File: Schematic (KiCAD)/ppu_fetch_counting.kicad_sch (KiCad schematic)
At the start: 28 parts

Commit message: - Started work on the pulse channels.  - Solved at least 2 of the red traces in the SVG.  - Finally realized that "Unknown 4to1" cells are actually just ordinary And-Or-Invert "AOI22" cells.
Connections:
- net at S7. (X): now also R9. (X); no longer S8. (/Q)
- net at S19. (X): now also R12. (X); no longer S20. (/Q)
- net at S11. (X): now also R10. (X); no longer S12. (/Q)
- net at S14. (X): now also R11. (X); no longer S15. (/Q)
- new net: S10. (X), S12. (/Q), S8. (/Q)
- new net: S22. (X), S23. (/Q), S26. (/Q), S27. (/Q), S28. (/Q)
- new net: S7. (X), S8. (/Q)
- new net: S19. (X), S20. (/Q)
- new net: S12. (/Q), S13. (X), S15. (/Q)
- new net: S11. (X), S12. (/Q)
- new net: R5. (/Q), S16. (X)
- new net: S14. (X), S15. (/Q)
- new net: S20. (/Q), S21. (X), S23. (/Q)

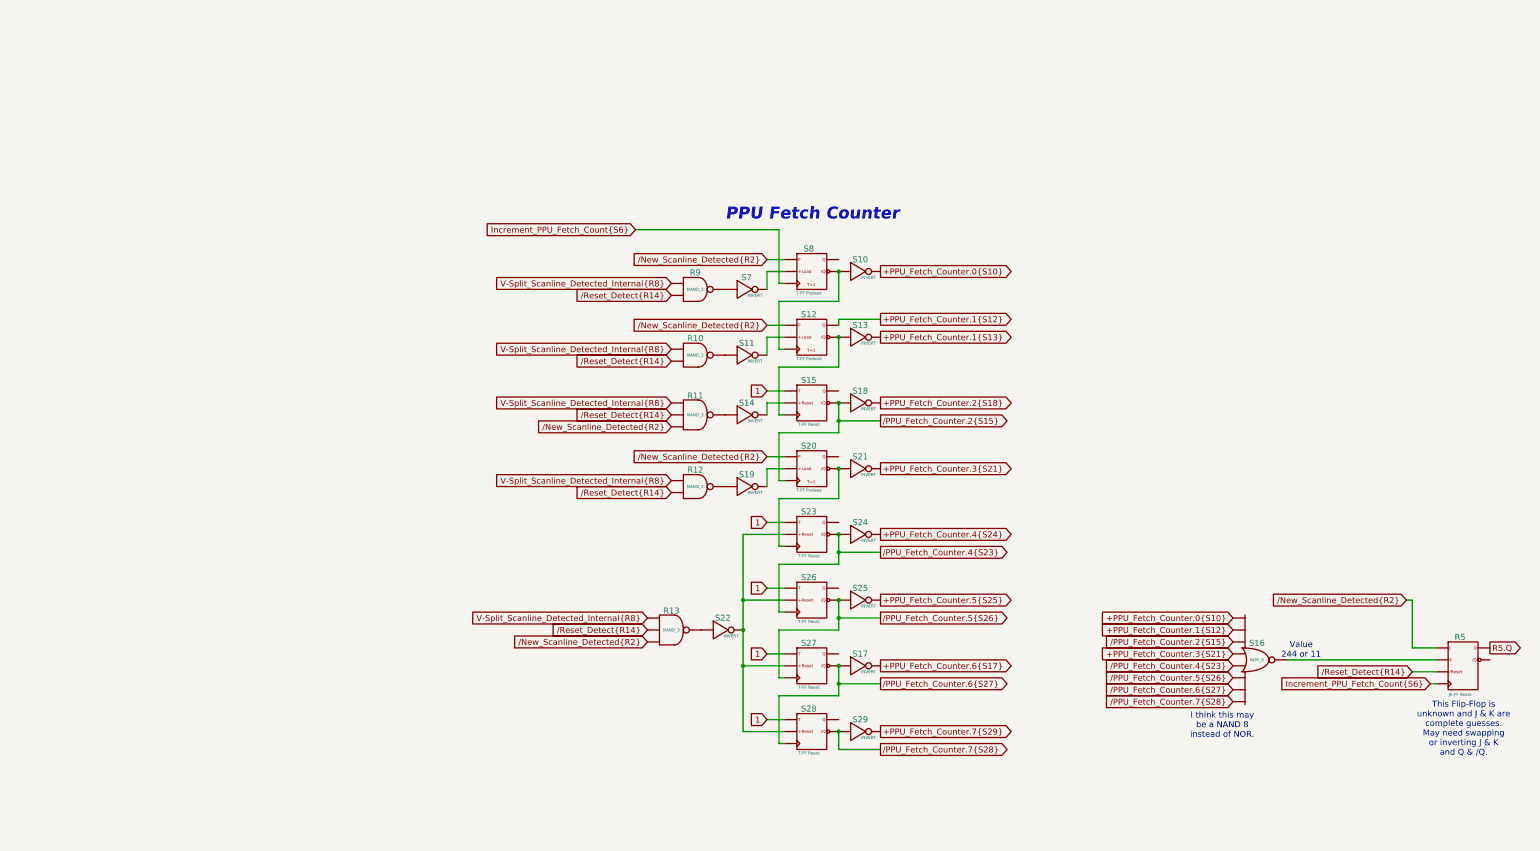
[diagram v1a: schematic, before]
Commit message: - All cells in the left and center areas have now been added into the schematics.  - Changed naming of the PDF files; I was accidentally writing over furrtek's original with my new PDF.
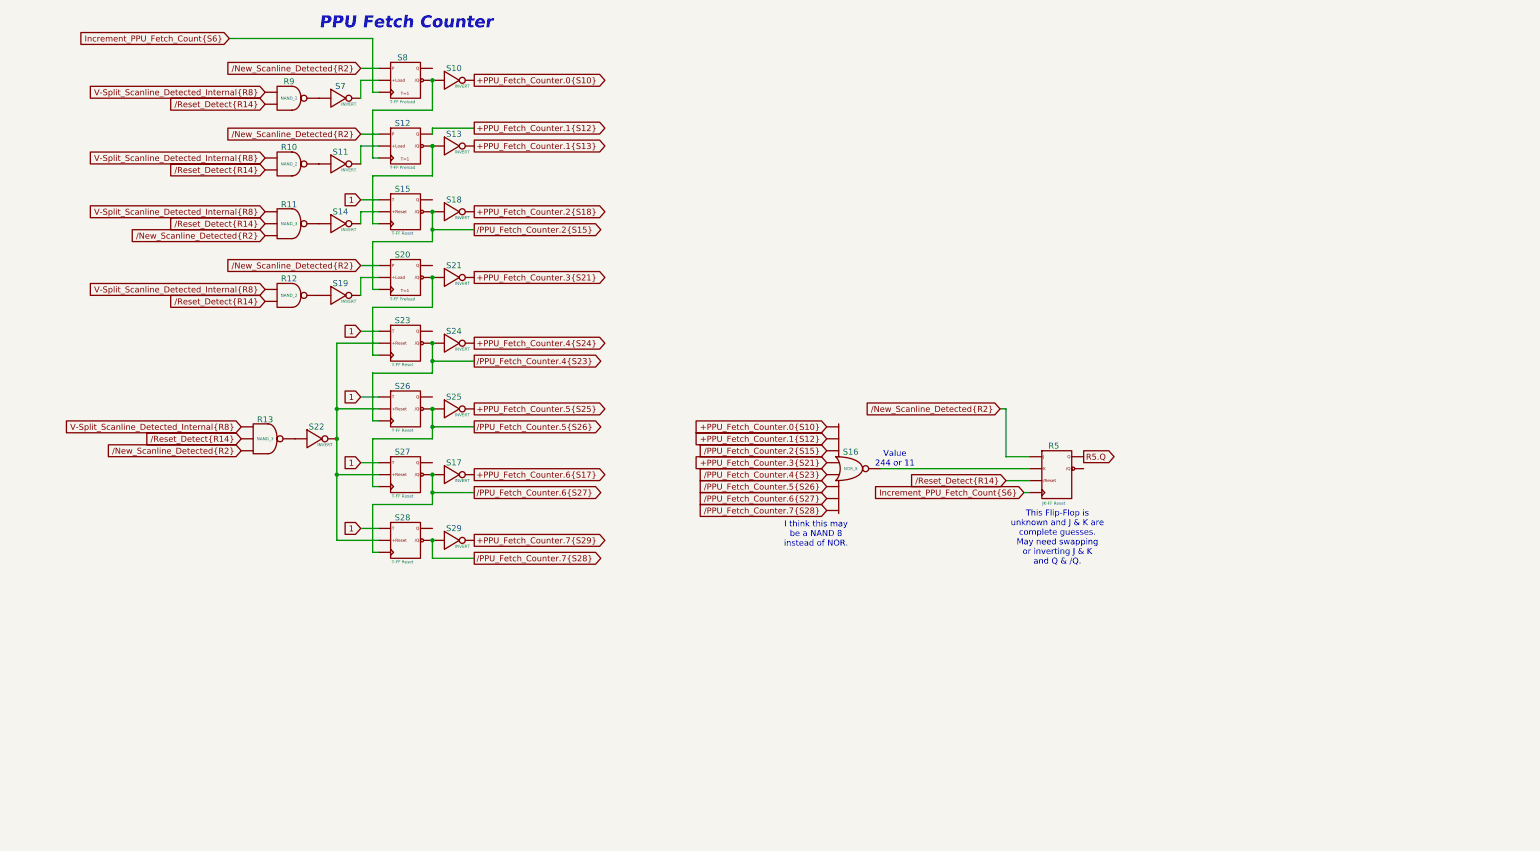
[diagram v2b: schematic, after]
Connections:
- net at S7. (X): now also R9. (X); no longer S8. (/Q)
- net at S19. (X): now also R12. (X); no longer S20. (/Q)
- net at S11. (X): now also R10. (X); no longer S12. (/Q)
- net at S14. (X): now also R11. (X); no longer S15. (/Q)
- new net: S10. (X), S12. (/Q), S8. (/Q)
- new net: S22. (X), S23. (/Q), S26. (/Q), S27. (/Q), S28. (/Q)
- new net: S7. (X), S8. (/Q)
- new net: S19. (X), S20. (/Q)
- new net: S12. (/Q), S13. (X), S15. (/Q)
- new net: S11. (X), S12. (/Q)
- new net: R5. (/Q), S16. (X)
- new net: S14. (X), S15. (/Q)
- new net: S20. (/Q), S21. (X), S23. (/Q)
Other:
- moved on the sheet: R10, R11, R12, R13, R5, R9, S10, S11, S12, S13, S14, S15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

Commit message: - All known gates and traces are now accounted for in the schematics!  :)
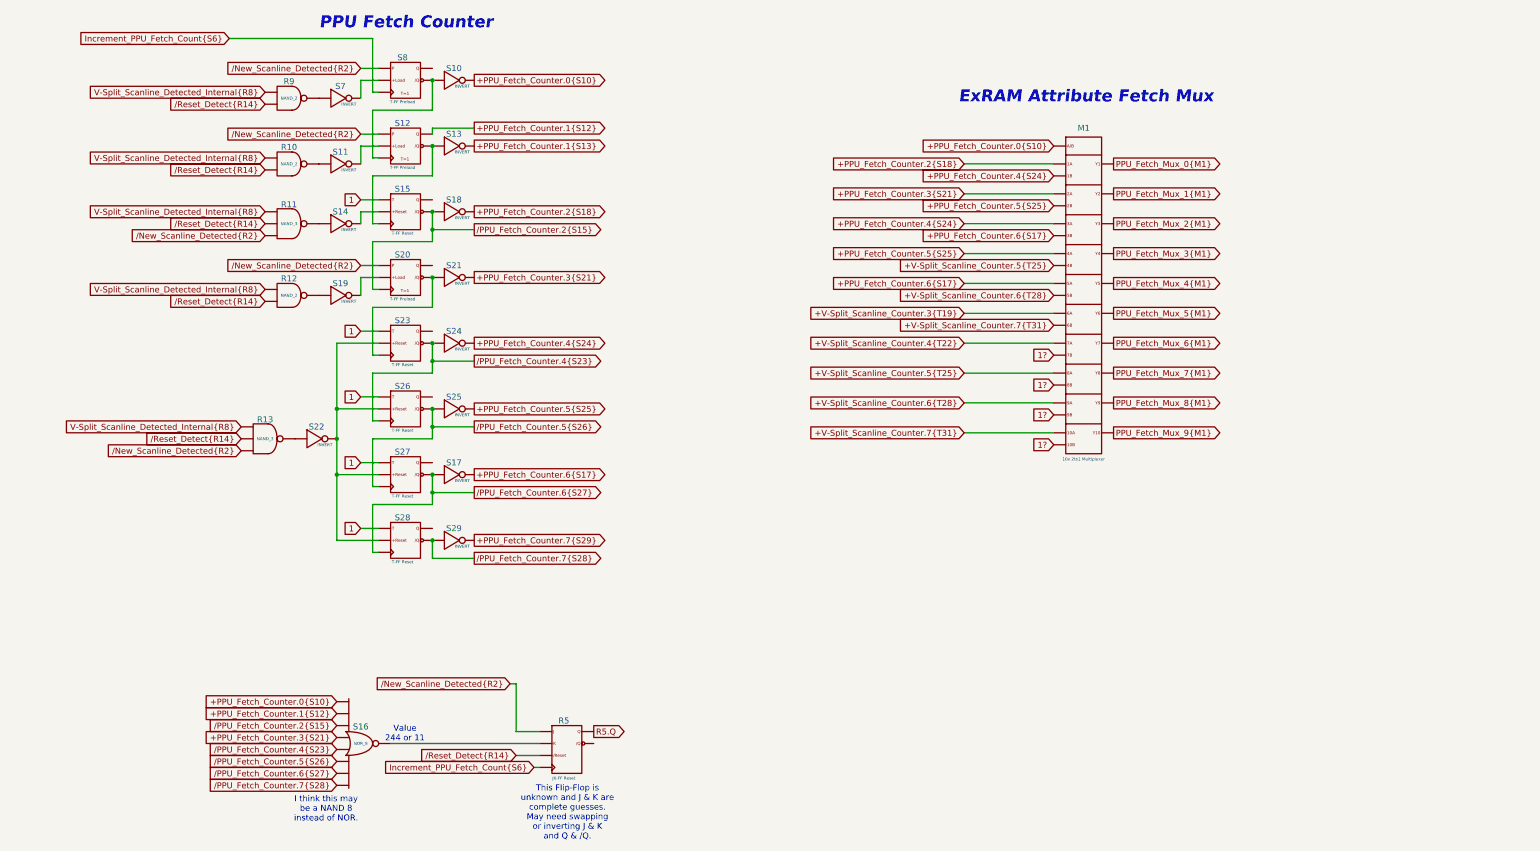
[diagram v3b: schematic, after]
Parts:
- added M1: 10x 2to1 Multiplexer, symbol MMC5:Multiplexer_10x2to1
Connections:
- net +PPU_Fetch_Counter.0{S10}: now also M1. (Y10)
- net +PPU_Fetch_Counter.2{S18}: now also M1. (Y10)
- net +PPU_Fetch_Counter.3{S21}: now also M1. (Y10)
- net +PPU_Fetch_Counter.4{S24}: now also M1. (Y10)
- net +PPU_Fetch_Counter.5{S25}: now also M1. (Y10)
- net +PPU_Fetch_Counter.6{S17}: now also M1. (Y10)
- net at S7. (X): now also R9. (X); no longer S8. (/Q)
- net at S19. (X): now also R12. (X); no longer S20. (/Q)
- net at S11. (X): now also R10. (X); no longer S12. (/Q)
- net at S14. (X): now also R11. (X); no longer S15. (/Q)
- new net: S10. (X), S12. (/Q), S8. (/Q)
- new net: S22. (X), S23. (/Q), S26. (/Q), S27. (/Q), S28. (/Q)
- new net: S7. (X), S8. (/Q)
- new net: S19. (X), S20. (/Q)
- new net: S12. (/Q), S13. (X), S15. (/Q)
- new net: S11. (X), S12. (/Q)
- new net: R5. (/Q), S16. (X)
- new net: S14. (X), S15. (/Q)
- new net: S20. (/Q), S21. (X), S23. (/Q)
- new net +V-Split_Scanline_Counter.3{T19}: M1. (Y10)
- new net +V-Split_Scanline_Counter.4{T22}: M1. (Y10)
- new net +V-Split_Scanline_Counter.5{T25}: M1. (Y10)
- new net +V-Split_Scanline_Counter.6{T28}: M1. (Y10)
- new net +V-Split_Scanline_Counter.7{T31}: M1. (Y10)
- new net 1?: M1. (Y10)
- new net PPU_Fetch_Mux_0{M1}: M1. (Y10)
- new net PPU_Fetch_Mux_1{M1}: M1. (Y10)
- new net PPU_Fetch_Mux_2{M1}: M1. (Y10)
- new net PPU_Fetch_Mux_3{M1}: M1. (Y10)
- new net PPU_Fetch_Mux_4{M1}: M1. (Y10)
- new net PPU_Fetch_Mux_5{M1}: M1. (Y10)
- new net PPU_Fetch_Mux_6{M1}: M1. (Y10)
- new net PPU_Fetch_Mux_7{M1}: M1. (Y10)
- new net PPU_Fetch_Mux_8{M1}: M1. (Y10)
- new net PPU_Fetch_Mux_9{M1}: M1. (Y10)
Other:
- note added: "ExRAM Attribute Fetch Mux"
- moved on the sheet: R5, S16
